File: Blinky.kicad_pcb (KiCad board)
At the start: 2 copper layers, 19 parts, among them Q1 IPD90P03P404ATMA2, Q2 IPD90P03P404ATMA2, U1 DCM4623TD2J13D0T70

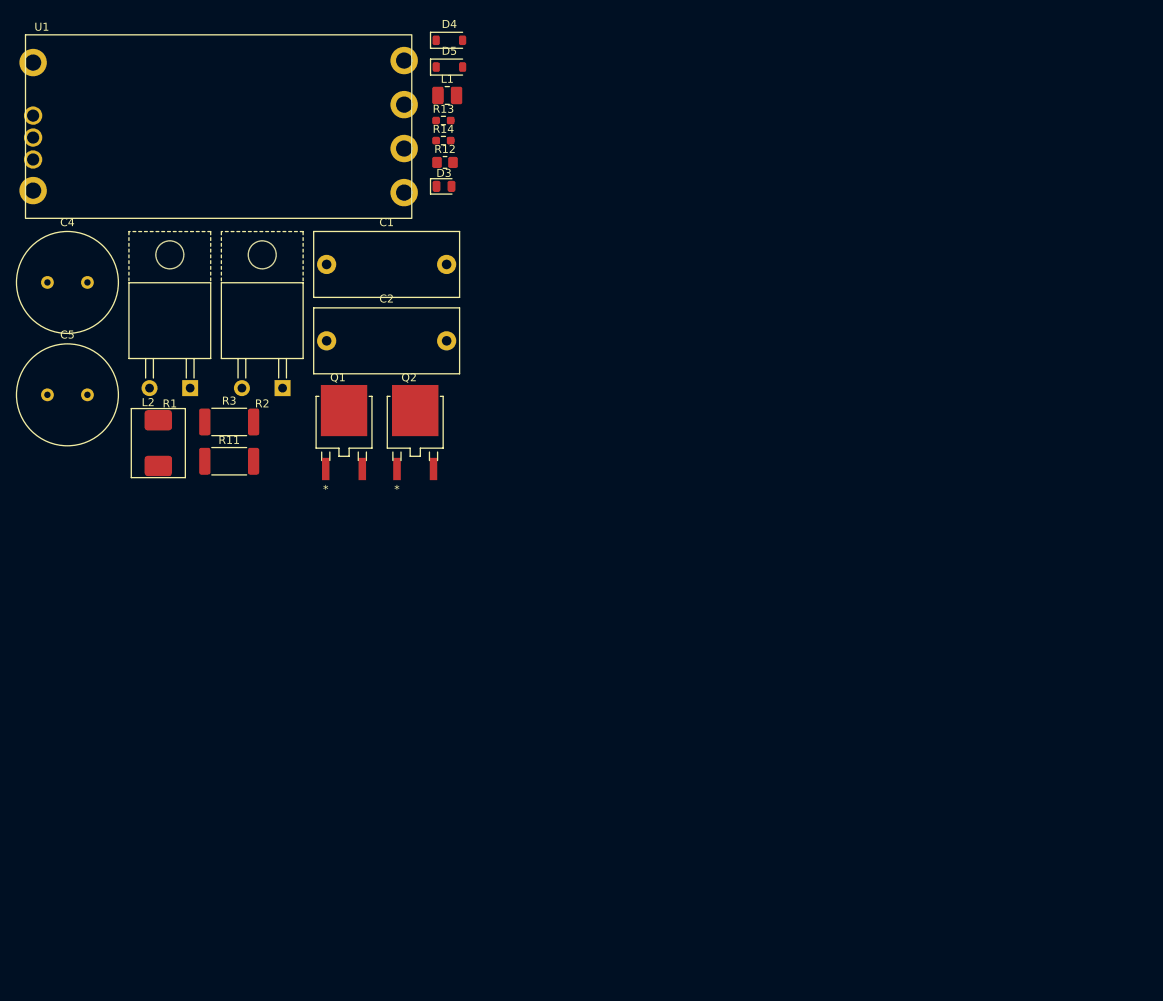
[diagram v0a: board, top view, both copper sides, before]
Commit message: further adjusted buck schematic
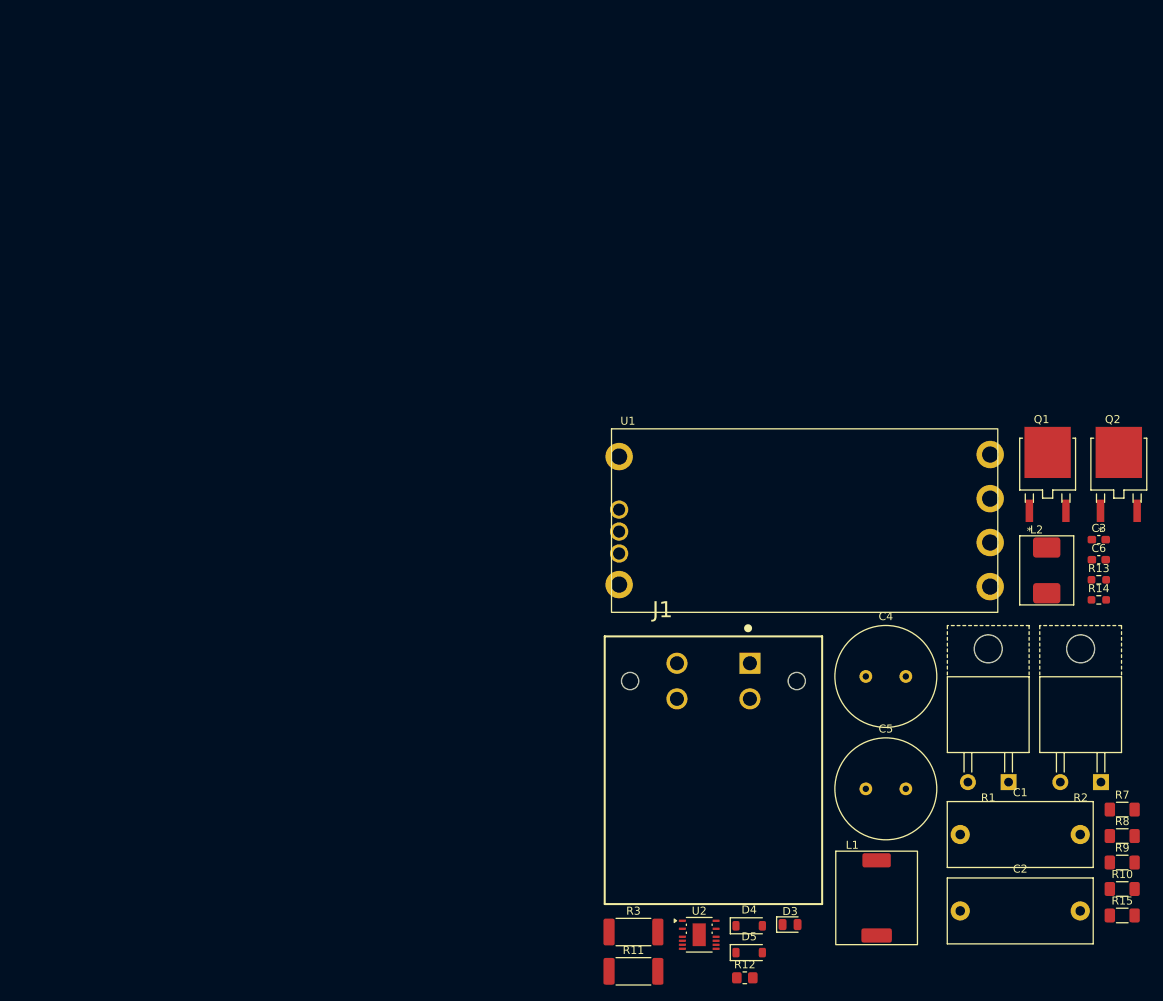
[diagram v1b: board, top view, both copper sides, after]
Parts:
- added C3: 47u, Capacitor_SMD:C_0603_1608Metric_Pad1.08x0.95mm_HandSolder, F.Cu at (135.4, 63.6)
- added C6: 1u, Capacitor_SMD:C_0603_1608Metric_Pad1.08x0.95mm_HandSolder, F.Cu at (135.4, 66.1)
- added J1: DTF13-4P-G003, AERO_Connectors:DTF13-4P-G003, F.Cu at (87.3, 81.3)
- added R10: 267k, Resistor_SMD:R_1206_3216Metric_Pad1.30x1.75mm_HandSolder, F.Cu at (138.4, 107.3)
- added R15: 196k, Resistor_SMD:R_1206_3216Metric_Pad1.30x1.75mm_HandSolder, F.Cu at (138.4, 110.6)
- added R7: R_US, Resistor_SMD:R_1206_3216Metric_Pad1.30x1.75mm_HandSolder, F.Cu at (138.4, 97.3)
- added R8: 10k, Resistor_SMD:R_1206_3216Metric_Pad1.30x1.75mm_HandSolder, F.Cu at (138.4, 100.6)
- added R9: 127k, Resistor_SMD:R_1206_3216Metric_Pad1.30x1.75mm_HandSolder, F.Cu at (138.4, 104.0)
- added U2: LTC3638xMSE, Package_SO:Analog_MSOP-12-16-1EP_3x4.039mm_P0.5mm_EP1.651x2.845mm, F.Cu at (85.5, 113.0)
- L1: value 1uH -> MSS1038-102; footprint Inductor_SMD:L_1008_2520Metric_Pad1.43x2.20mm_HandSolder -> AERO_Inductors:MSS1038-102
- moved D4 116.9 mm to (91.7, 111.9)
- moved D5 116.9 mm to (91.7, 115.2)
- moved L1 113.8 mm to (107.7, 108.4)
- moved R2 113.5 mm to (133.2, 82.3)
- moved C4 113.5 mm to (106.3, 80.7)
- moved C5 113.5 mm to (106.3, 94.7)
- moved R1 113.5 mm to (121.6, 82.3)
- moved L2 112.2 mm to (128.9, 67.4)
- moved R12 108.6 mm to (91.2, 118.4)
- moved C1 106.5 mm to (118.1, 100.5)
- moved C2 106.5 mm to (118.1, 110.0)
- moved D3 101.9 mm to (96.9, 111.7)
- moved R13 100.0 mm to (135.4, 68.6)
- moved R14 100.0 mm to (135.4, 71.1)
- moved U1 88.3 mm to (98.7, 61.2)
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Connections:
- net Net-(U1-+IN) renamed /VICOR_IN

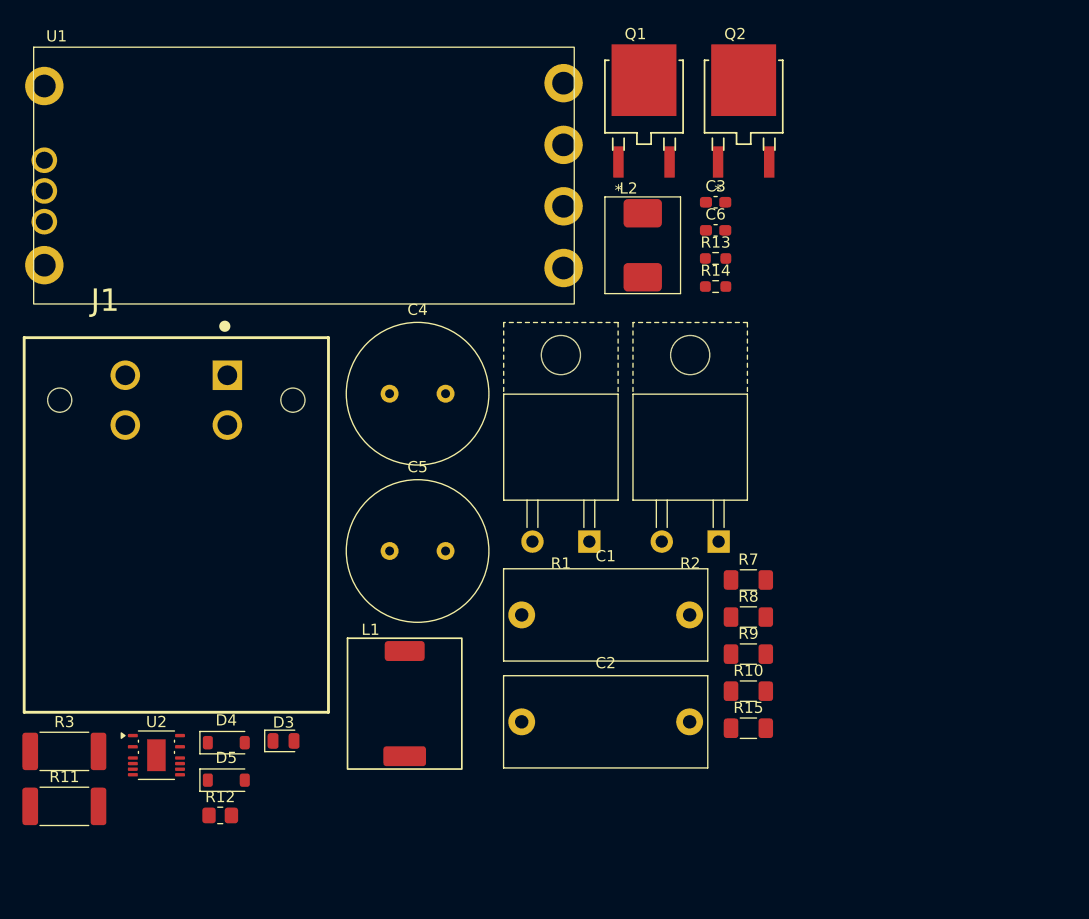
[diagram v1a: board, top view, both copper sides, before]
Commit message: added second VICOR
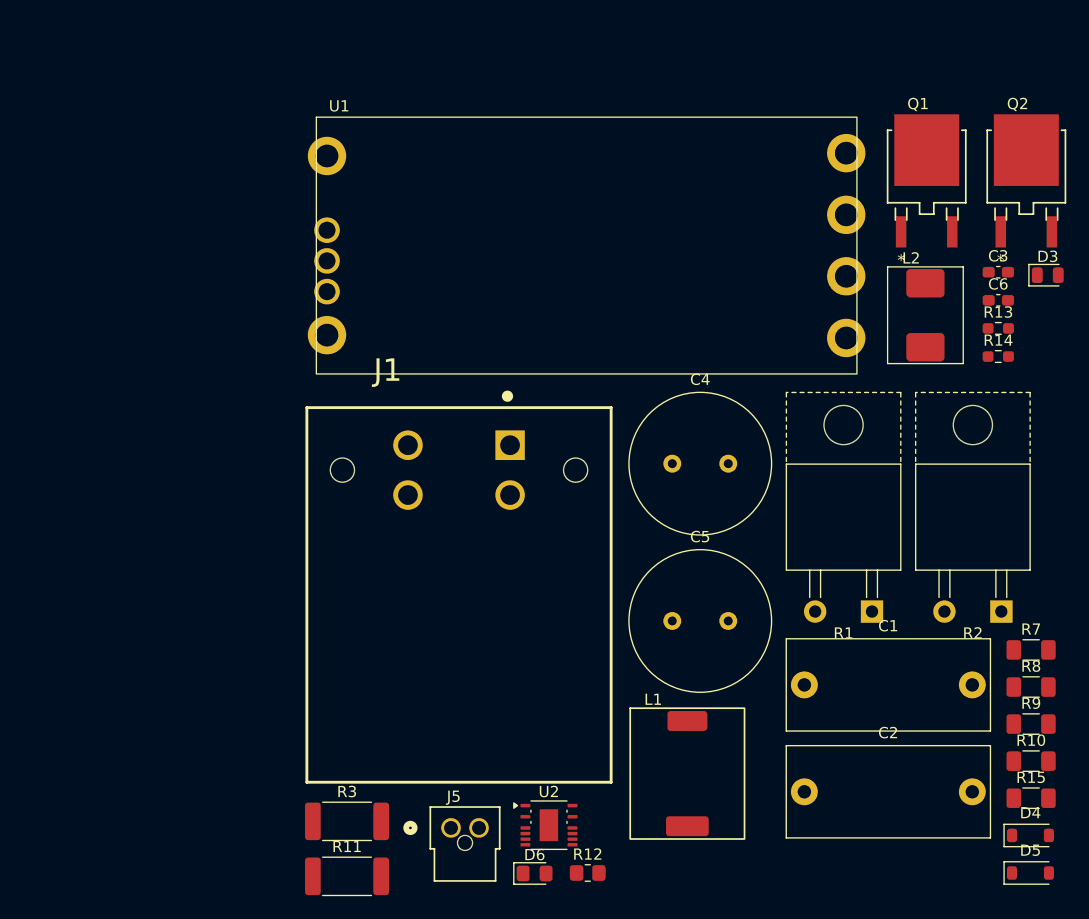
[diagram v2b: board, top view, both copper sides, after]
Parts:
- added D6: LED, LED_SMD:LED_0805_2012Metric_Pad1.15x1.40mm_HandSolder, F.Cu at (119.3, 123.5)
- added J5: 1053091102, AERO_Connectors:1053091102, F.Cu at (113.1, 119.5)
- moved D3 79.9 mm to (165.1, 70.1)
- moved D4 72.3 mm to (163.6, 120.2)
- moved D5 72.3 mm to (163.6, 123.5)
- moved U2 35.6 mm to (120.6, 119.2)
- moved R12 33.2 mm to (124.0, 123.5)
- moved C1 26.0 mm to (143.4, 106.7)
- moved C2 26.0 mm to (143.4, 116.3)
- moved C3 26.0 mm to (160.7, 69.8)
- moved C6 26.0 mm to (160.7, 72.4)
- moved J1 26.0 mm to (112.5, 87.5)
- moved L1 26.0 mm to (132.9, 114.6)
- moved L2 26.0 mm to (154.2, 73.7)
- moved Q1 26.0 mm to (154.3, 60.4)
- moved Q2 26.0 mm to (163.2, 60.4)
- moved R1 26.0 mm to (146.9, 88.5)
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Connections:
- net Net-(D2-K) renamed /SW
- net Net-(D6-A) renamed /BUCK_OUT
- net Net-(U2-RUN) renamed /BUCK_IN
- net Net-(U2-VFB) renamed /FB
- U2 pad 10: Net-(U2-SS) -> unconnected-(U2-SS-Pad10)
- U2 pad 7: Net-(U2-SS) -> /INVERTER-

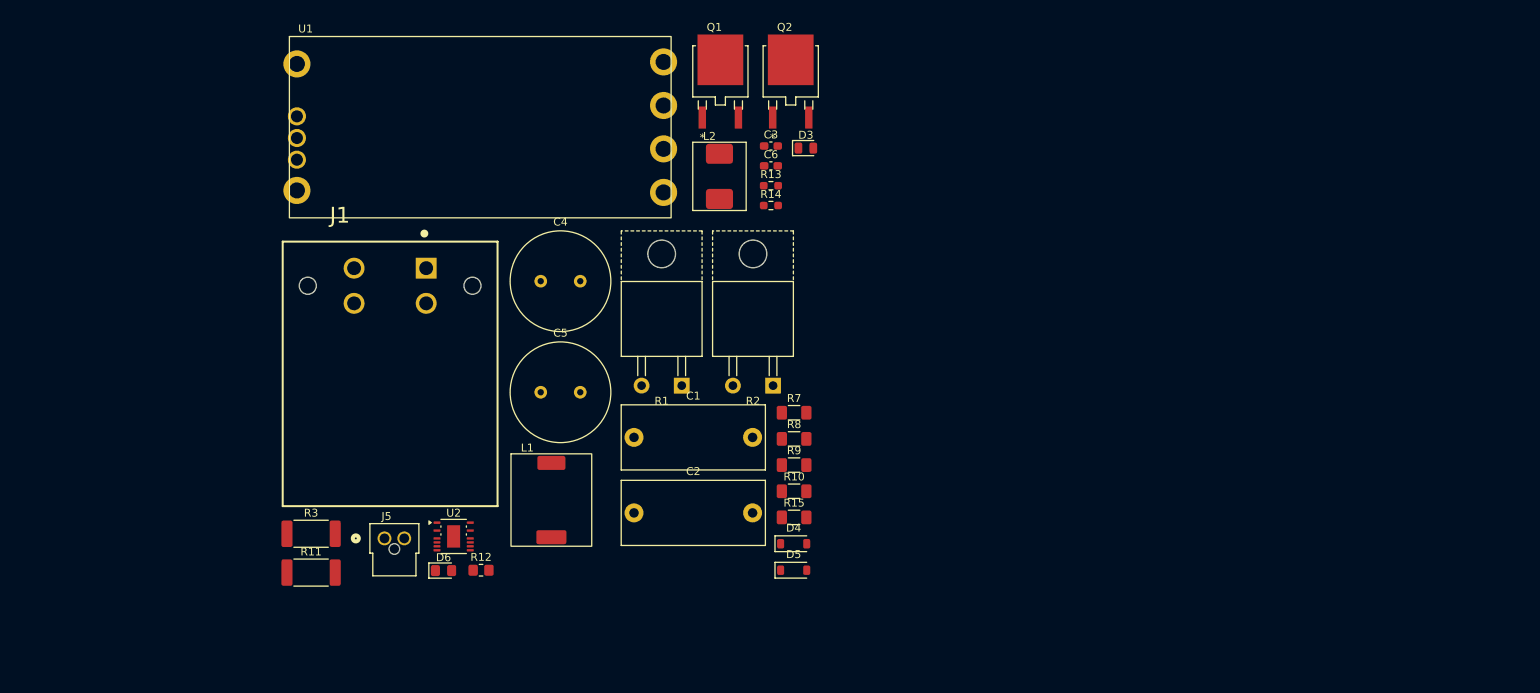
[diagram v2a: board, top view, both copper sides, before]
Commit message: Started layout
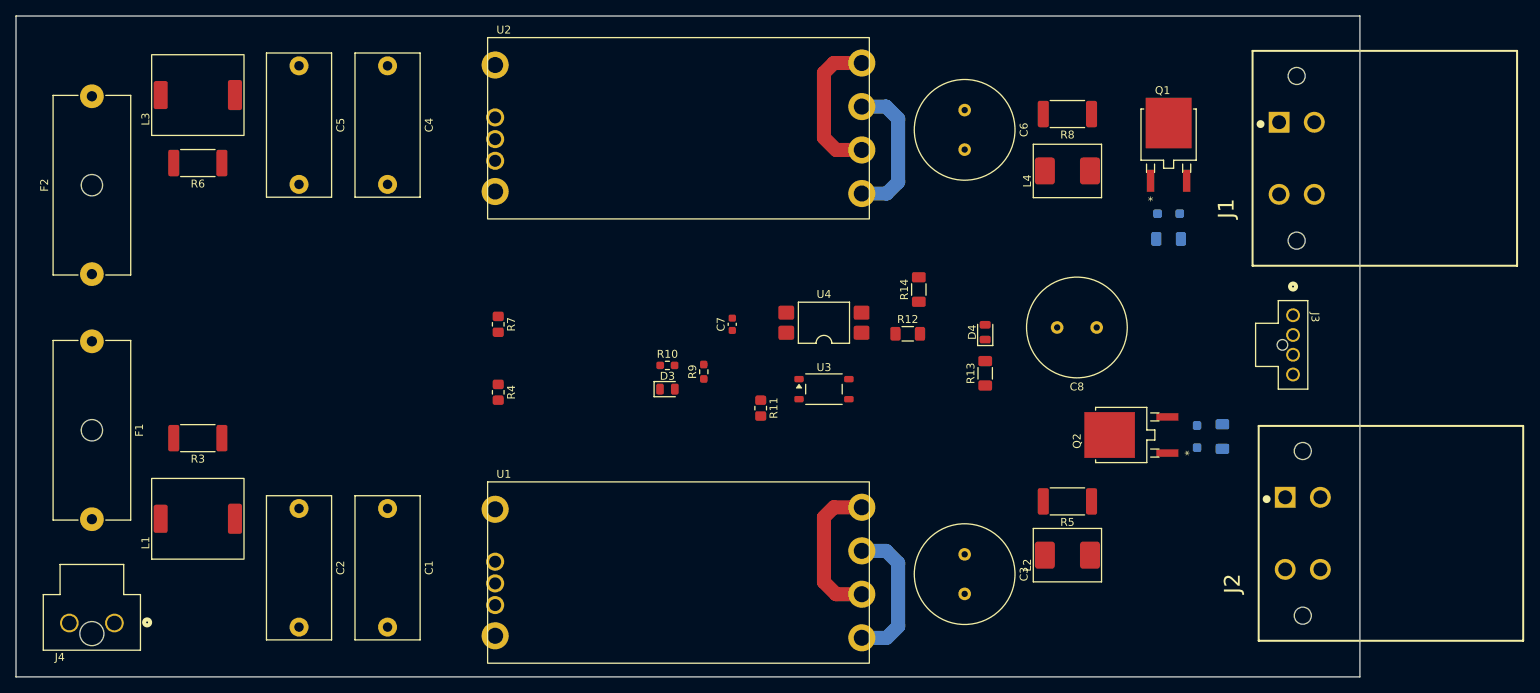
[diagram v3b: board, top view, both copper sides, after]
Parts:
- removed D5: BZT52C5V1, Diode_SMD:D_SOD-123
- removed D6: LED, LED_SMD:LED_0805_2012Metric_Pad1.15x1.40mm_HandSolder
- removed J5: 1053091102, AERO_Connectors:1053091102
- removed R15: 196k, Resistor_SMD:R_1206_3216Metric_Pad1.30x1.75mm_HandSolder
- added C7: 0.1u, Capacitor_SMD:C_0603_1608Metric, F.Cu at (155.8, 92.4)
- added C8: 100u, Capacitor_THT:C_Radial_D12.5mm_H25.0mm_P5.00mm, F.Cu at (201.9, 92.8)
- added D1: BZT52C5V1, Diode_SMD:D_SOD-123F, B.Cu at (214.6, 106.6)
- added D2: BZT52C5V1, Diode_SMD:D_SOD-123F, B.Cu at (211.0, 78.4)
- added F1: 0031.8201, Fuse:Fuseholder_Cylinder-5x20mm_Schurter_0031_8201_Horizontal_Open, F.Cu at (74.8, 94.5)
- added F2: 0031.8201, Fuse:Fuseholder_Cylinder-5x20mm_Schurter_0031_8201_Horizontal_Open, F.Cu at (74.8, 86.0)
- added J2: DTF13-4P-G003, AERO_Connectors:DTF13-4P-G003, F.Cu at (228.0, 118.8)
- added J3: 1053091104, AERO_Connectors:1053091104, F.Cu at (226.7, 95.0)
- added J4: 2002411132, AERO_Connectors:2002411132, F.Cu at (74.8, 130.1)
- added L3: MSS1038-102, AERO_Inductors:MSS1038-102, F.Cu at (88.2, 63.4)
- added L4: SLC7649S-151KLC, AERO_Inductors:SLC7649S-151KLC, F.Cu at (198.2, 73.0)
- added R4: 301, Resistor_SMD:R_0805_2012Metric_Pad1.20x1.40mm_HandSolder, F.Cu at (126.2, 101.0)
- added R5: 1, Resistor_SMD:R_2512_6332Metric_Pad1.40x3.35mm_HandSolder, F.Cu at (198.2, 114.8)
- added R6: 1, Resistor_SMD:R_2512_6332Metric_Pad1.40x3.35mm_HandSolder, F.Cu at (88.2, 72.0)
- added U3: TLP184, Package_SO:Toshiba_SOIC-4-6_4.4x3.6mm_P1.27mm, F.Cu at (167.4, 100.6)
- added U4: LTV-817S, Package_DIP:SMDIP-4_W9.53mm, F.Cu at (167.4, 92.2)
- C3: value 47u -> 4700uF; footprint Capacitor_SMD:C_0603_1608Metric_Pad1.08x0.95mm_HandSolder -> Capacitor_THT:C_Radial_D12.5mm_H25.0mm_P5.00mm
- C4: value 4700uF -> 1uF; footprint Capacitor_THT:C_Radial_D12.5mm_H25.0mm_P5.00mm -> Capacitor_THT:C_Rect_L18.0mm_W8.0mm_P15.00mm_FKS3_FKP3
- C5: value 100uF -> 1uF; footprint Capacitor_THT:C_Radial_D12.5mm_H25.0mm_P5.00mm -> Capacitor_THT:C_Rect_L18.0mm_W8.0mm_P15.00mm_FKS3_FKP3
- C6: value 1u -> 4700uF; footprint Capacitor_SMD:C_0603_1608Metric_Pad1.08x0.95mm_HandSolder -> Capacitor_THT:C_Radial_D12.5mm_H25.0mm_P5.00mm
- D4: value BZT52C5V1 -> LTST-C171KRKT; footprint Diode_SMD:D_SOD-123 -> LED_SMD:LED_0805_2012Metric
- R1, R2: value MP925-5.00K-1% -> 22k; footprint AERO_Resistors:MP925-5.00K-1%_TabUp -> Resistor_SMD:R_1206_3216Metric_Pad1.30x1.75mm_HandSolder; moved to B.Cu
- R10: value 267k -> 50k; footprint Resistor_SMD:R_1206_3216Metric_Pad1.30x1.75mm_HandSolder -> Resistor_SMD:R_0603_1608Metric_Pad0.98x0.95mm_HandSolder
- R11: value 1 -> R_0805; footprint Resistor_SMD:R_2512_6332Metric_Pad1.40x3.35mm_HandSolder -> Resistor_SMD:R_0805_2012Metric_Pad1.20x1.40mm_HandSolder
- R12: footprint Resistor_SMD:R_0805_2012Metric_Pad1.20x1.40mm_HandSolder -> Resistor_SMD:R_1206_3216Metric_Pad1.30x1.75mm_HandSolder
- R13: value 22k -> 500; footprint Resistor_SMD:R_0603_1608Metric_Pad0.98x0.95mm_HandSolder -> Resistor_SMD:R_1206_3216Metric_Pad1.30x1.75mm_HandSolder
- R14: value 22k -> 1k; footprint Resistor_SMD:R_0603_1608Metric_Pad0.98x0.95mm_HandSolder -> Resistor_SMD:R_1206_3216Metric_Pad1.30x1.75mm_HandSolder
- R7: value R_US -> 301; footprint Resistor_SMD:R_1206_3216Metric_Pad1.30x1.75mm_HandSolder -> Resistor_SMD:R_0805_2012Metric_Pad1.20x1.40mm_HandSolder
- R8: value 10k -> 1; footprint Resistor_SMD:R_1206_3216Metric_Pad1.30x1.75mm_HandSolder -> Resistor_SMD:R_2512_6332Metric_Pad1.40x3.35mm_HandSolder
- R9: value 127k -> 1k; footprint Resistor_SMD:R_1206_3216Metric_Pad1.30x1.75mm_HandSolder -> Resistor_SMD:R_0603_1608Metric_Pad0.98x0.95mm_HandSolder
- U1: value DCM4623TD2J13D0T70 -> DCM4623TD2J13D0T00; footprint AERO_Regulators:DCM4623TD2J13D0T70 -> AERO_Regulators:DCM4623TD2J13D0T00
- U2: value LTC3638xMSE -> DCM4623TD2J13D0T00; footprint Package_SO:Analog_MSOP-12-16-1EP_3x4.039mm_P0.5mm_EP1.651x2.845mm -> AERO_Regulators:DCM4623TD2J13D0T00
- moved J1 115.8 mm to (227.2, 71.4), turned to 90 degrees
- moved R1 73.2 mm to (217.8, 106.6), turned to -90 degrees
- moved L2 65.1 mm to (198.2, 121.6), turned to 90 degrees
- moved Q2 62.2 mm to (205.0, 106.4), turned to 90 degrees
- moved R12 61.7 mm to (178.0, 93.6)
- moved U1 61.7 mm to (149.0, 123.8)
- moved R11 60.6 mm to (159.4, 103.0), turned to -90 degrees
- moved U2 58.9 mm to (149.0, 67.6)
- moved Q1 57.3 mm to (211.0, 68.4)
- moved C3 57.2 mm to (185.2, 121.5), turned to -90 degrees
- moved R8 53.7 mm to (198.2, 65.8), turned to 180 degrees
- moved R2 53.0 mm to (211.0, 81.6), turned to 180 degrees
- moved C5 51.4 mm to (101.0, 59.7), turned to -90 degrees
- moved L1 44.8 mm to (88.2, 117.0), turned to 90 degrees
- moved C2 42.4 mm to (101.0, 115.7), turned to -90 degrees
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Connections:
- net /VICOR_IN renamed /VICOR-1/VICOR_IN
- C1 pad 2: /INVERTER- -> /Control Signals/INVERTER-
- C2 pad 2: /INVERTER- -> /Control Signals/INVERTER-
- C3 pad 1: /BUCK_OUT -> /VICOR-1/VICOR_RAW
- C3 pad 2: /INVERTER- -> LV_GND
- C4 pad 1: /VICOR_RAW -> /VICOR-2/VICOR_IN
- C4 pad 2: LV_GND -> /Control Signals/INVERTER-
- C5 pad 1: /VICOR_FILTERED -> /VICOR-2/VICOR_IN
- C5 pad 2: LV_GND -> /Control Signals/INVERTER-
- C6 pad 1: /BUCK_IN -> /VICOR-2/VICOR_RAW
- C6 pad 2: /INVERTER- -> LV_GND
- D3 pad 1: Net-(D3-K) -> /Control Signals/INVERTER-
- D3 pad 2: /VICOR_FILTERED -> Net-(D3-A)
- D4 pad 1: /VICOR_OUT -> Net-(D4-K)
- D4 pad 2: Net-(D4-A) -> TSMS12V
- J1 pad 1: /VICOR_OUT -> /GLV Connectors/VICOR_OUT
- J1 pad 2: /VICOR_OUT -> /GLV Connectors/VICOR_OUT
- J1 pad 3: /VICOR_OUT -> /GLV Connectors/VICOR_OUT
- J1 pad 4: /VICOR_OUT -> /GLV Connectors/VICOR_OUT
- L1 pad 1: /INVERTER+ -> Net-(F1-Pad2)
- L2 pad 1: /VICOR_RAW -> /VICOR-1/VICOR_RAW
- L2 pad 2: /VICOR_FILTERED -> /GLV Connectors/VICOR_FILTERED
- Q1 pad 1: /VICOR_FILTERED -> /GLV Connectors/VICOR_FILTERED
- Q1 pad 2: Net-(D4-A) -> Net-(D1-A)
- Q1 pad 3: /VICOR_OUT -> /GLV Connectors/VICOR_OUT
- Q2 pad 1: /VICOR_FILTERED -> /GLV Connectors/VICOR_FILTERED
- Q2 pad 2: Net-(D5-A) -> Net-(D2-A)
- Q2 pad 3: /VICOR_OUT -> /GLV Connectors/VICOR_OUT
- R1 pad 1: /PRECHARGE_RELAY -> LV_GND
- R1 pad 2: /INVERTER+ -> Net-(D1-A)
- R10 pad 1: /BUCK_OUT -> /Control Signals/INVERTER-
- R10 pad 2: /FB -> Net-(D3-A)
- R11 pad 1: /VICOR_FILTERED -> Net-(R11-Pad1)
- R11 pad 2: /VICOR_RAW -> /Control Signals/INVERTER-
- R12 pad 1: Net-(D3-K) -> Net-(R12-Pad1)
- R12 pad 2: LV_GND -> /Control Signals/LV_EN
- R13 pad 1: Net-(D4-A) -> /Control Signals/~{LV_FAULT}
- R13 pad 2: LV_GND -> Net-(D4-K)
- R14 pad 1: Net-(D5-A) -> /Control Signals/LV_EN
- R14 pad 2: LV_GND -> TSMS12V
- R2 pad 1: /INVERTER- -> LV_GND
- R2 pad 2: /PRECHARGE_RELAY -> Net-(D2-A)
- R3 pad 2: /INVERTER+ -> Net-(F1-Pad2)
- R7 pad 1: Net-(D6-K) -> /VICOR-2/HV_TRIM
- R7 pad 2: /INVERTER- -> /Control Signals/INVERTER-
- R8 pad 1: /BUCK_IN -> /GLV Connectors/VICOR_FILTERED
- R8 pad 2: /INVERTER- -> /VICOR-2/VICOR_RAW
- R9 pad 1: /INVERTER+ -> /Control Signals/HV_FAULT
- R9 pad 2: /BUCK_IN -> Net-(D3-A)
- U1 pad 2: /TRIM_HV -> /VICOR-1/HV_TRIM
- U1 pad 3: /EN_HV -> /Control Signals/HV_EN
- U1 pad 4: /FAULT_HV -> /Control Signals/HV_FAULT
- U1 pad 5: /INVERTER- -> /Control Signals/INVERTER-
- U1 pad 8: /VICOR_RAW -> /VICOR-1/VICOR_RAW
- U2 pad 1: /SW -> /VICOR-2/VICOR_IN
- U2 pad 3: /BUCK_IN -> /Control Signals/HV_EN
- U2 pad 5: unconnected-(U2-FBO-Pad5) -> /Control Signals/INVERTER-
- U2 pad 8: /INVERTER- -> /VICOR-2/VICOR_RAW
- U2 pad 9: /FB -> LV_GND
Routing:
- net LV_GND: track 0.00 -> 36.9 mm
- net /VICOR-2/VICOR_RAW: track 0.00 -> 18.9 mm
- net /VICOR-1/VICOR_RAW: track 0.00 -> 18.9 mm
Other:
- board outline added: 170 x 83.6 mm
